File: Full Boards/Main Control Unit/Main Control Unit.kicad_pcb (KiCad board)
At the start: 4 copper layers, 350 x 200 mm, 405 parts, among them J1 Optional Bond, J2 Future Use, J3 Conn_01x02_Pin, Q1 DMN6075S, Q10 DMN6075S, Q11 BSS314PE, Q12 DMN6075S, Q13 BSS314PE, Q14 DMN6075S, Q15 DMN6075S, Q2 BSS314PE, Q3 DMN6075S, Q4 BSS314PE, Q5 DMN6075S, Q6 DMN6075S, Q7 DMN6075S, Q8 DMN6075S, Q9 BSS314PE, SW1 Boot, SW2 Reset, T1 760390014, T2 760390014

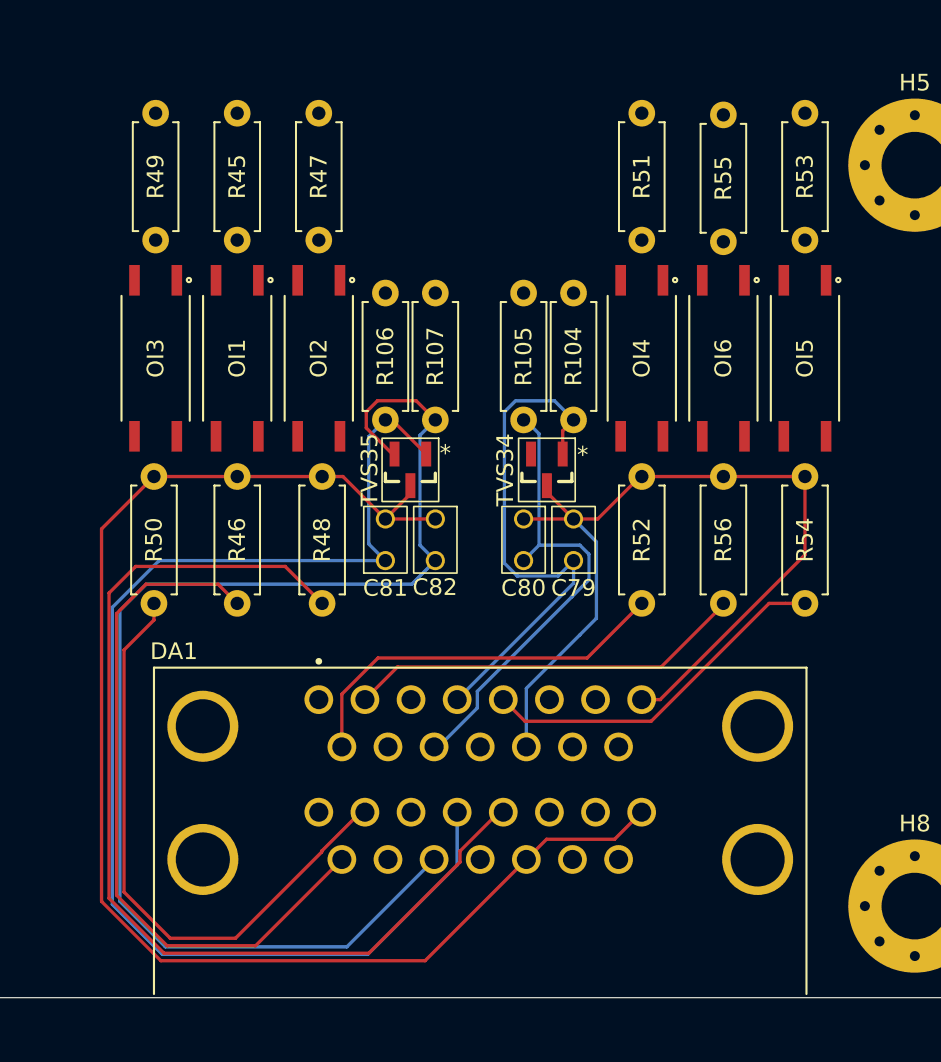
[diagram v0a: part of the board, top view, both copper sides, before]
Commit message: Started reworking the DA1 connection's PCB layout.
Signed-off-by: digimer <digital.mermaid@gmail.com>
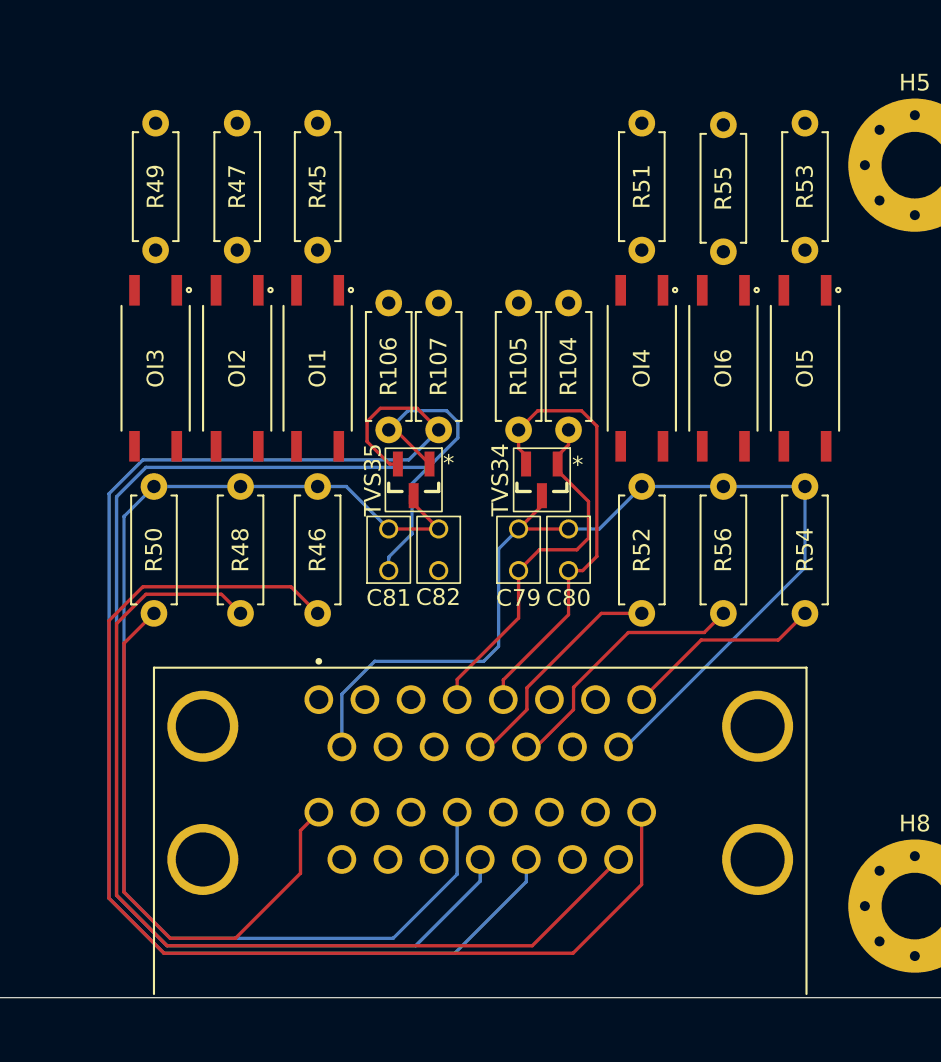
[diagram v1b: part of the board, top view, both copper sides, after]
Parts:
- moved R48 4.94 mm to (259.5, 269.3)
- moved R47 4.94 mm to (259.3, 255.1)
- moved OI2 4.94 mm to (259.3, 262.2)
- moved R46 4.87 mm to (264.1, 269.3)
- moved R45 4.87 mm to (264.1, 255.1)
- moved OI1 4.87 mm to (264.1, 262.2)
- moved C79 3.35 mm to (276.2, 273.1)
- moved C80 2.77 mm to (279.2, 273.1)
- moved R104 0.67 mm to (279.2, 265.9)
- moved R105 0.67 mm to (276.2, 265.9)
- moved TVS34 0.67 mm to (277.6, 268.9)
- moved C81 0.63 mm to (268.4, 273.1)
- moved C82 0.63 mm to (271.4, 273.1)
- moved R106 0.63 mm to (268.4, 265.9)
- moved R107 0.63 mm to (271.4, 265.9)
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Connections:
- DA1 pad 1: M5KW_12V -> /M5KW_LOW_SW_CTRL
- DA1 pad 10: /M5KW_CANBUS_HIGH -> M5KW_5V
- DA1 pad 11: /M5KW_REGEN_DAC_PLUG -> M5KW_5V
- DA1 pad 12: M5KW_5V -> /M5KW_THROTTLE_DAC_PLUG
- DA1 pad 13: M5KW_GND -> /M5KW_REGEN_DAC_PLUG
- DA1 pad 15: M5KW_5V -> /M5KW_FOOT_SW_CTRL
- DA1 pad 17: /M10KW_LOW_SW_CTRL -> M10KW_5V
- DA1 pad 18: /M10KW_CANBUS_LOW -> M10KW_5V
- DA1 pad 2: /M5KW_LOW_SW_CTRL -> /M5KW_CANBUS_LOW
- DA1 pad 20: /M10KW_FOOT_SW_CTRL -> /M10KW_REGEN_DAC_PLUG
- DA1 pad 23: M10KW_GND -> /M10KW_FOOT_SW_CTRL
- DA1 pad 24: /M10KW_HIGH_SW_CTRL -> M10KW_GND
- DA1 pad 25: /M10KW_CANBUS_HIGH -> /M10KW_CANBUS_LOW
- DA1 pad 26: /M10KW_REGEN_DAC_PLUG -> /M10KW_CANBUS_HIGH
- DA1 pad 27: M10KW_5V -> /M10KW_HIGH_SW_CTRL
- DA1 pad 28: M10KW_GND -> /M10KW_LOW_SW_CTRL
- DA1 pad 3: /M5KW_CANBUS_LOW -> /M5KW_CANBUS_HIGH
- DA1 pad 30: M10KW_5V -> M10KW_GND
- DA1 pad 4: /M5KW_THROTTLE_DAC_PLUG -> M5KW_GND
- DA1 pad 5: /M5KW_FOOT_SW_CTRL -> M5KW_GND
- DA1 pad 8: M5KW_GND -> /M5KW_HIGH_SW_CTRL
- DA1 pad 9: /M5KW_HIGH_SW_CTRL -> M5KW_12V
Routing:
- net /M5KW_HIGH_SW_CTRL: track 42.3 -> 70.1 mm
- net /M5KW_THROTTLE_DAC_PLUG: track 75.3 -> 88.6 mm
- net M5KW_GND: track 85.0 -> 72.9 mm
- net /M10KW_THROTTLE_DAC_PLUG: track 32.4 -> 21.8 mm
- net /M10KW_HIGH_SW_CTRL: track 23.7 -> 13.8 mm
- net /M10KW_FOOT_SW_CTRL: track 21.6 -> 12.0 mm
- net M10KW_GND: track 54.7 -> 62.8 mm
- net /M10KW_LOW_SW_CTRL: track 24.0 -> 15.9 mm
- net /M5KW_REGEN_DAC_PLUG: track 77.3 -> 84.0 mm
- net /M5KW_FOOT_SW_CTRL: track 61.7 -> 58.5 mm
- net /M5KW_LOW_SW_CTRL: track 36.9 -> 35.0 mm
- net /M10KW_REGEN_DAC_PLUG: track 28.1 -> 27.0 mm

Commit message: Saving progress post crash, pre-recovery.
Signed-off-by: digimer <digital.mermaid@gmail.com>
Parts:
- moved IOX1 94.2 mm to (273.8, 246.5), turned to -90 degrees
- moved J2 75.8 mm to (294.0, 224.2)
- moved R44 60.6 mm to (277.8, 236.0), turned to 180 degrees
- moved OI5 0.70 mm to (294.1, 262.2)
- moved OI3 0.70 mm to (253.7, 262.2)
- moved OI1 0.70 mm to (263.4, 262.2)
- moved OI2 0.70 mm to (258.6, 262.2)
- moved OI4 0.70 mm to (284.3, 262.2)
- moved OI6 0.70 mm to (289.2, 262.2)
- moved R55 0.63 mm to (288.3, 254.6)
- moved R51 0.54 mm to (283.4, 254.6)
- moved R45 0.54 mm to (264.3, 254.6)
- moved R47 0.54 mm to (259.5, 254.6)
- moved R49 0.54 mm to (254.6, 254.6)
- moved R53 0.54 mm to (293.2, 254.6)
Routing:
- net Net-(IOX1-P0): track 0.00 -> 48.3 mm
- net Net-(IOX1-P5): track 0.00 -> 38.8 mm
- net Net-(IOX1-P2): track 0.00 -> 27.9 mm
- net Net-(IOX1-P4): track 0.00 -> 24.1 mm
- net Net-(IOX1-P1): track 0.00 -> 20.0 mm
- net Net-(IOX1-P3): track 0.00 -> 15.7 mm
- net Net-(OI6-A): track 0.00 -> 3.81 mm
- net Net-(OI5-A): track 0.00 -> 3.81 mm
- net Net-(OI4-A): track 0.00 -> 3.81 mm
- net GND: track 0.00 -> 1.49 mm, vias 0 -> 1
